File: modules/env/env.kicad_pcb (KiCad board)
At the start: 2 copper layers, 30.5 x 68.6 mm, 29 parts, among them SW1 GATE MODE SELECT, SW2 ALGO MODE SELECT, U1 MCP6002-xSN, U2 ATtiny1616-M, U3 MCP6002-xSN

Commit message: env: introduce envelope generator. This is a digital envelope generator which has multiple modes to support different needs. Currently it has three modes/algorithms It also support MIDI and as well as usual Gate & CV
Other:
- board text added: "ENV 0.1.0"
- board text removed: "GATE 0.1.0"
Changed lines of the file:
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@@
 		)
 	)
-	(gr_text "GATE\n0.1.0"
+	(gr_text "ENV\n0.1.0"
 		(at 76.327 107.95 0)
 		(layer "F.SilkS")
@@
 		)
 	)
-	(gr_text "GATE"
-		(at 58.547 48.768 0)
+	(gr_text "ENV"
+		(at 59.182 48.641 0)
 		(layer "F.SilkS")
 		(effects

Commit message: env_1.0.0
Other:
- board text added: "ENV 1.0.0"
- board text removed: "ENV 0.1.0"
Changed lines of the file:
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@@
 		)
 	)
-	(gr_text "ENV\n0.1.0"
+	(gr_text "ENV\n1.0.0"
 		(at 76.327 107.95 0)
 		(layer "F.SilkS")

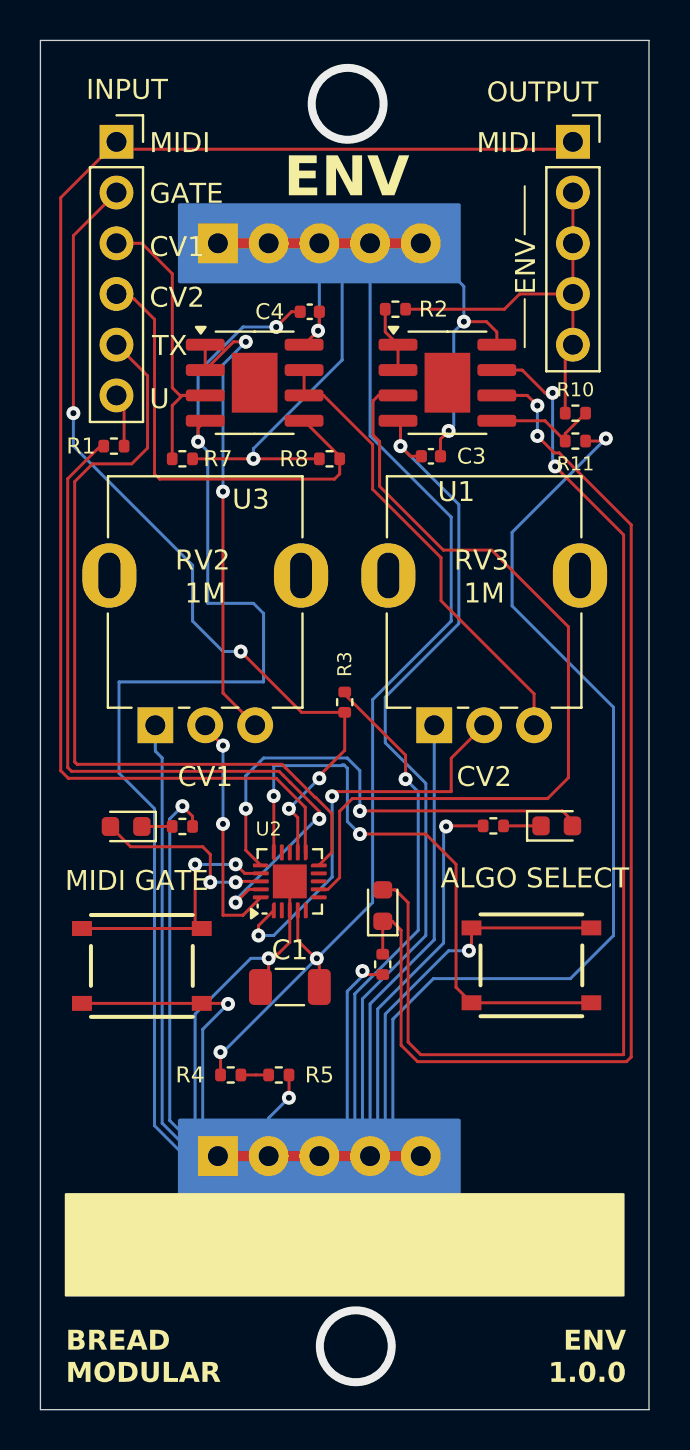
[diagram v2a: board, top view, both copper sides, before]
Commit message: Use a better button
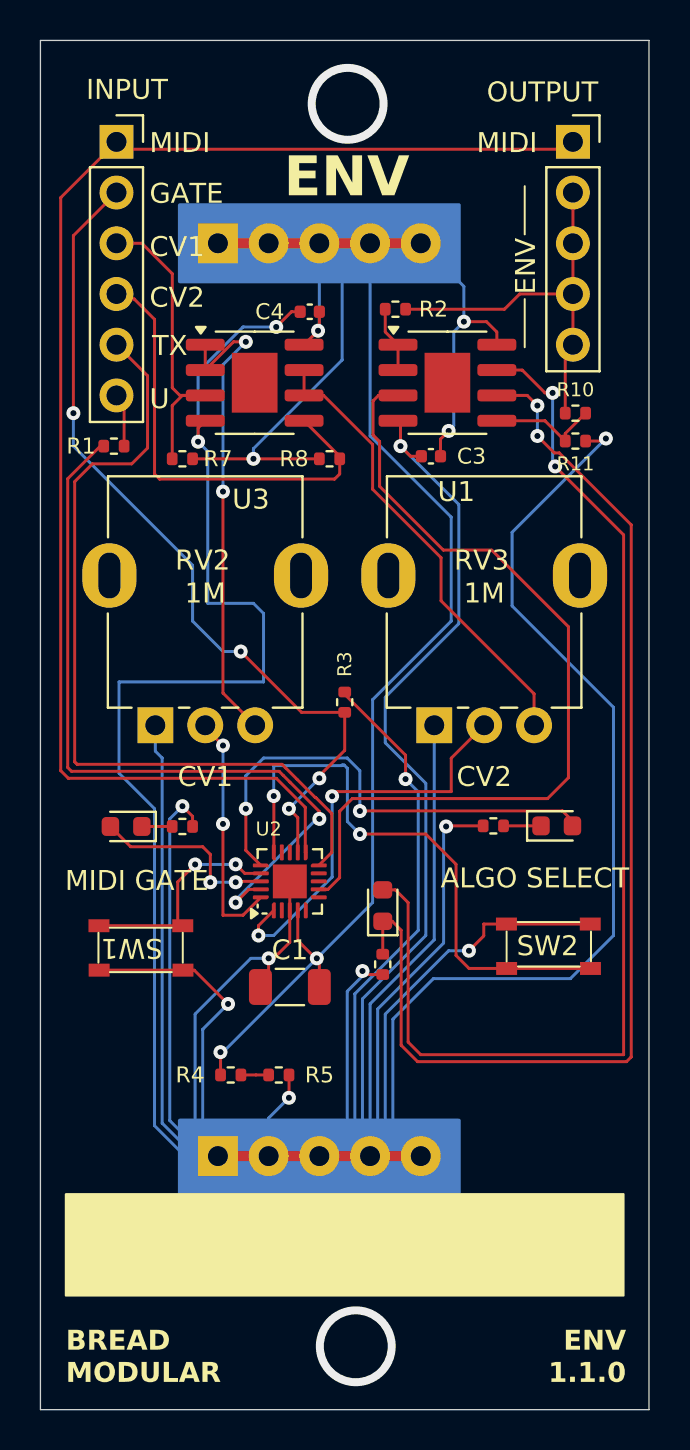
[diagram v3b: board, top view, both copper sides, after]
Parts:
- D1: value GATE MODE LED -> LED
- D2: value ALGO MODE LED -> LED
- D3: value ENV LED -> LED
- SW1: value GATE MODE SELECT -> K2-1808SN-A4SW-01; footprint BreadModular_MISC:SPST_TS-1187A-B-A-B -> BreadModular_MISC:K2-1808SN-A4SW-01
- SW2: value ALGO MODE SELECT -> K2-1808SN-A4SW-01; footprint BreadModular_MISC:SPST_TS-1187A-B-A-B -> BreadModular_MISC:K2-1808SN-A4SW-01
- moved SW2 1.26 mm to (72.4, 86.0)
- moved SW1 0.89 mm to (52.1, 86.1)
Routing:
- net Net-(SW1-B): track 12.8 -> 11.1 mm
- net Net-(SW2-B): track 30.4 -> 28.7 mm
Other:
- board text added: "ENV 1.1.0"
- board text removed: "ENV 1.0.0"
